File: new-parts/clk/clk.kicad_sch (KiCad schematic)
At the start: 10 parts, among them J1 Conn_02x02_Odd_Even, J2 Conn_01x08, K1 J104D2C12VDC.15S, K2 J104D2C12VDC.15S

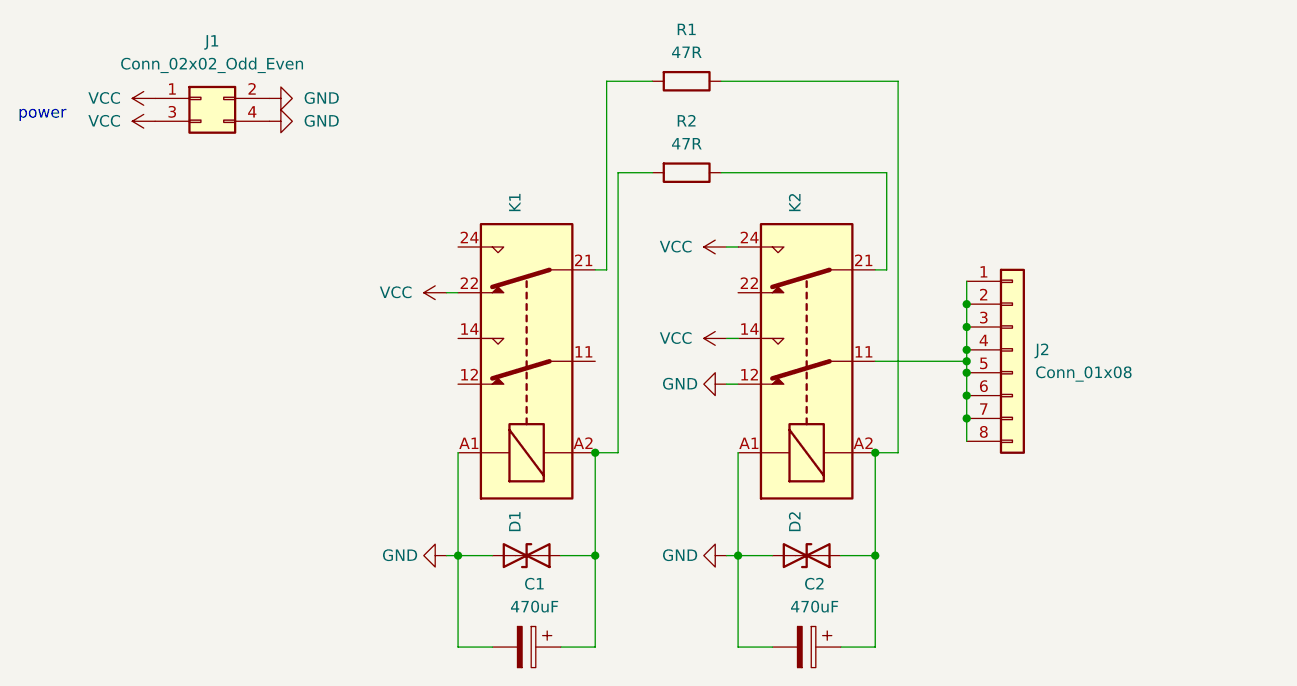
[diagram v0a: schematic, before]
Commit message: clk: Add trimming resistors.
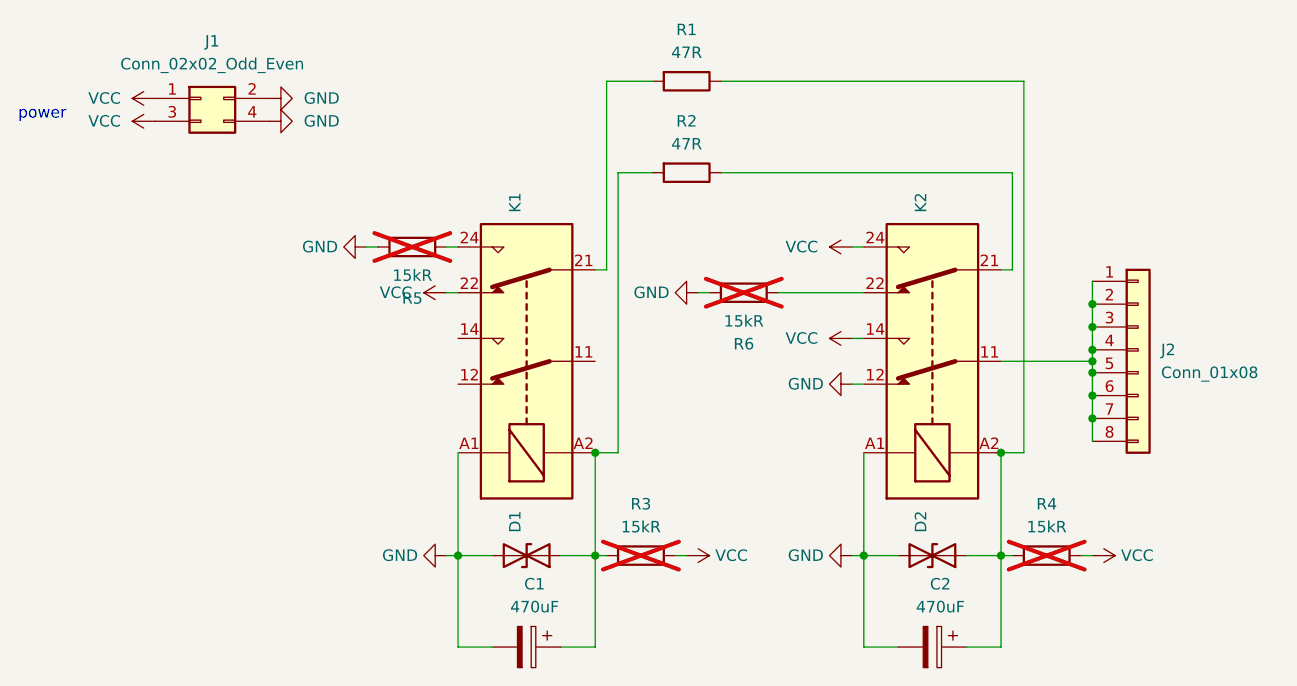
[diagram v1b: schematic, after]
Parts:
- added R3, R4, R5, R6: 15kR, Resistor_THT:R_Axial_DIN0204_L3.6mm_D1.6mm_P2.54mm_Vertical, symbol Device:R
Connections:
- net GND: now also R5.1, R6.1
- net VCC: now also R3.1, R4.1
- net at C1.1, D1.1 (A1), K1.A2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: now also R3.2
- net at C2.1, D2.1 (A1), K2.A2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: now also R4.2
- net at K1.24: now also R5.2
- net at K2.22: now also R6.2
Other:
- moved on the sheet: C2, D2, J2, K2
